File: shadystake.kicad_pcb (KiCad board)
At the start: 2 copper layers, 127 x 76.2 mm, 7 parts, among them J1 6P6C, J2 6P6C, J3 6P6C, J4 6P6C, J5 6P6C, J6 6P6C, J7 8P8C

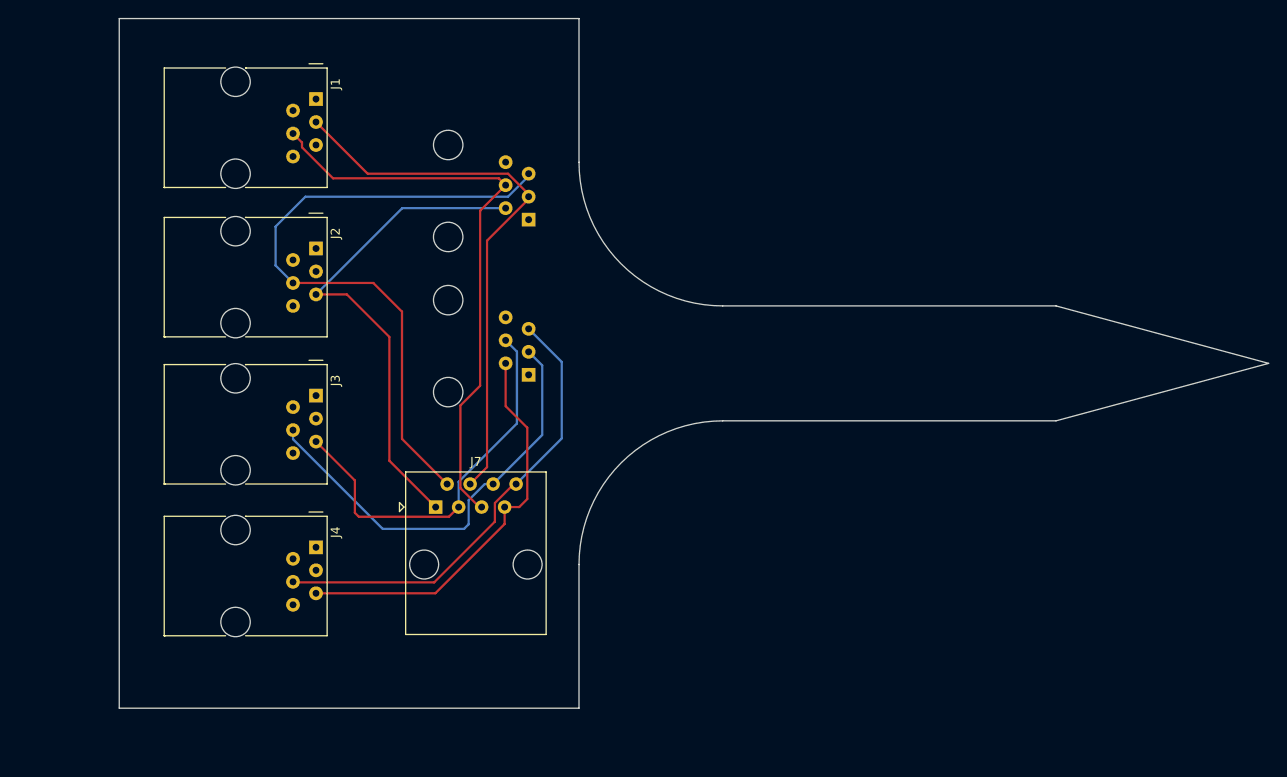
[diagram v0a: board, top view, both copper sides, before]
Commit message: shadystake: make it roughly the proportions of the Shadytel logo
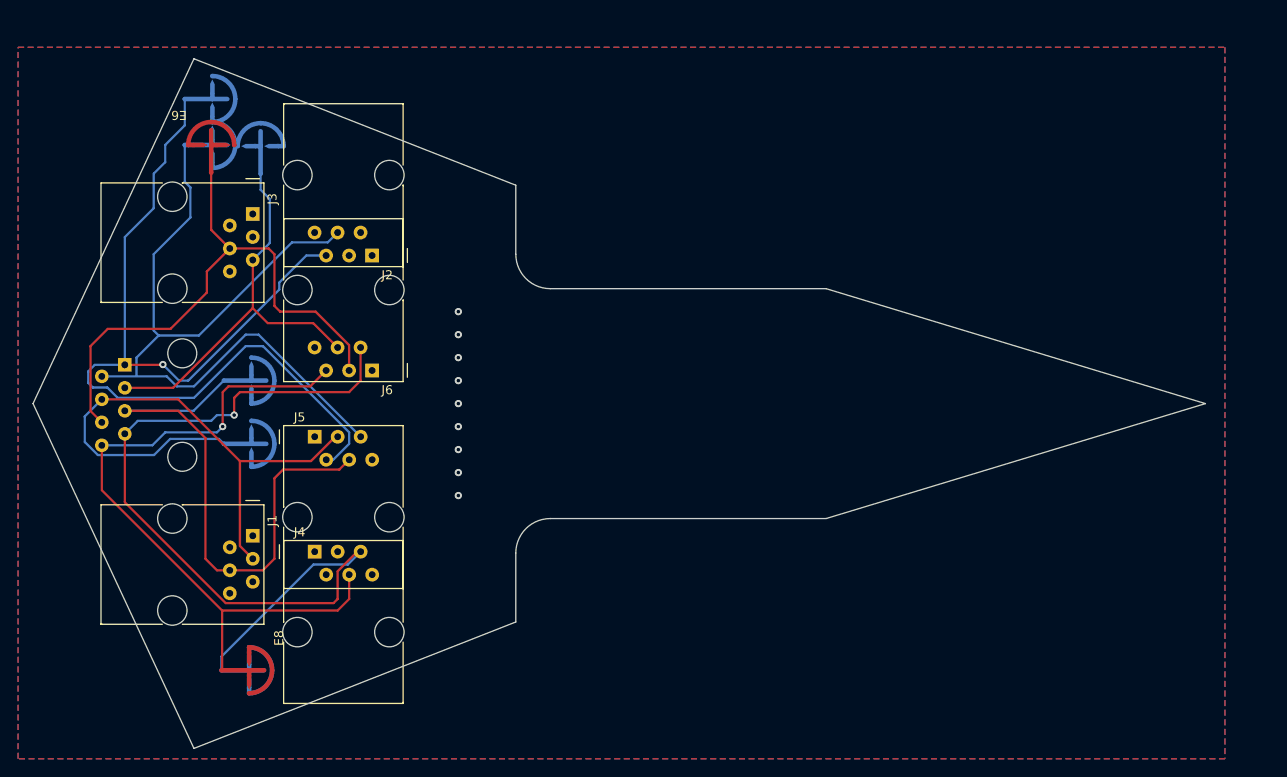
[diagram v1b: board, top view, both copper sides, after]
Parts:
- added E1: SPARK_GAP, Shadystake:Sparkgap_JLC, B.Cu at (72.4, 111.8)
- added E2: SPARK_GAP, Shadystake:Sparkgap_JLC, B.Cu at (72.4, 118.7)
- added E3: SPARK_GAP, Shadystake:Sparkgap_JLC, B.Cu at (68.1, 80.6)
- added E4: SPARK_GAP, Shadystake:Sparkgap_JLC, B.Cu at (68.1, 85.7)
- added E5: SPARK_GAP, Shadystake:Sparkgap_JLC, B.Cu at (73.4, 85.9)
- added E6: SPARK_GAP, Shadystake:Sparkgap_JLC, F.Cu at (67.9, 85.7)
- added E7: SPARK_GAP, Shadystake:Sparkgap_JLC, B.Cu at (72.1, 143.8)
- added E8: SPARK_GAP, Shadystake:Sparkgap_JLC, F.Cu at (72.1, 143.8)
- J5, J6: moved to F.Cu
- J7: moved to B.Cu
- moved J1 48.8 mm to (72.5, 128.9)
- moved J7 37.8 mm to (58.4, 110.0), turned to -90 degrees
- moved J5 33.7 mm to (79.4, 118.0), turned to 0 degrees
- moved J3 21.2 mm to (72.5, 93.3)
- moved J6 17.3 mm to (85.7, 110.6), turned to 180 degrees
- moved J2 6.24 mm to (85.7, 97.9), turned to 180 degrees
- moved J4 0.50 mm to (79.4, 130.7), turned to 0 degrees
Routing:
- net /TIP4: track 44.7 -> 97.0 mm, vias 0 -> 1
- net /TIP2: track 55.9 -> 107.3 mm, vias 0 -> 1
- net /RING4: track 50.8 -> 78.1 mm, vias 0 -> 1
- net /RING2: track 72.0 -> 89.2 mm
- net /RING3: track 48.3 -> 63.2 mm
- net /RING1: track 61.0 -> 63.5 mm
- net /TIP1: track 64.7 -> 62.5 mm
- net /TIP3: track 43.3 -> 45.0 mm
- net GND: vias 0 -> 9
- added copper zone on B.Cu, net GND
- added copper zone on F.Cu, net GND
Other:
- board size 127 x 76.2 mm -> 129.5 x 76.2 mm

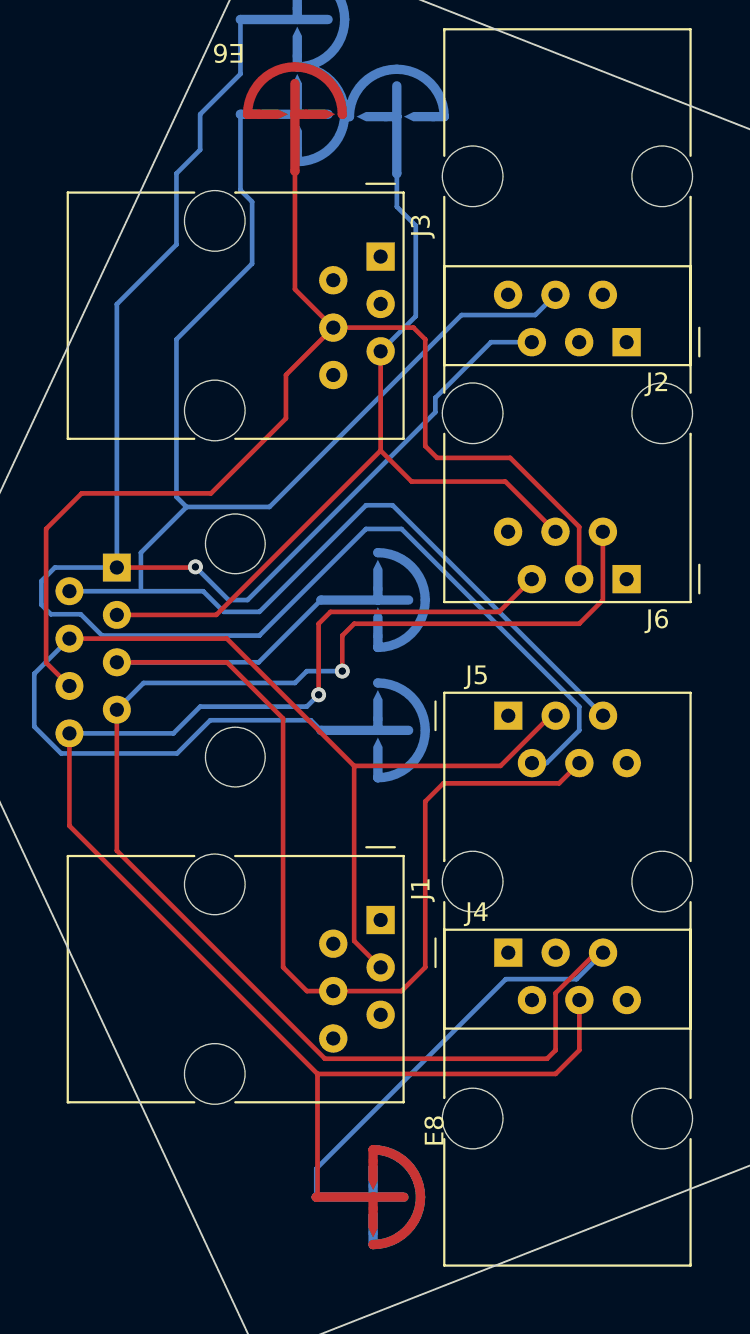
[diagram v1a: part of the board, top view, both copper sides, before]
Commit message: pcb: add copper labels on the "wrong" side of the board
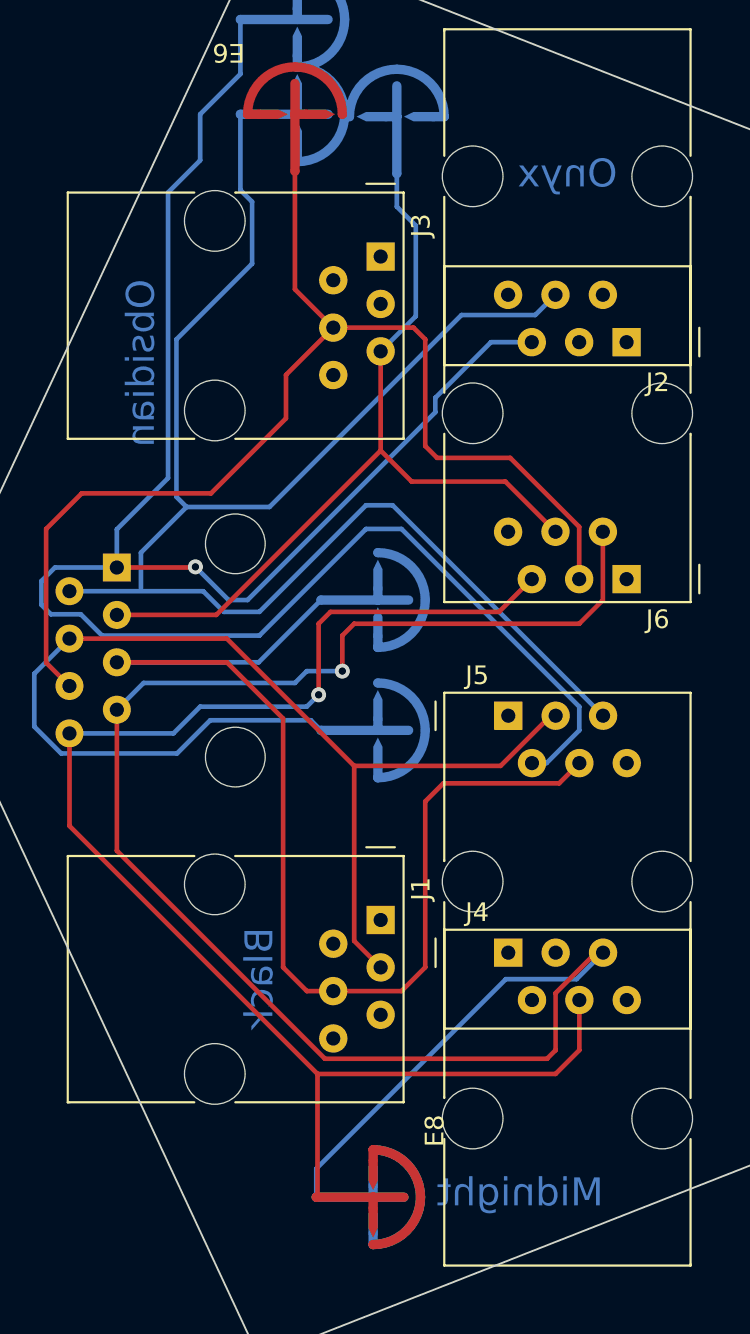
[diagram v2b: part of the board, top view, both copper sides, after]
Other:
- board text added: "Black"
- board text added: "Midnight"
- board text added: "Obsidian"
- board text added: "Onyx"
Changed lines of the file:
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@@
   (gr_arc (start 105.41 101.6) (mid 102.715923 100.484077) (end 101.6 97.79) (layer "Edge.Cuts") (width 0.1))
   (gr_line (start 101.6 130.81) (end 101.6 138.43) (layer "Edge.Cuts") (width 0.1))
+  (gr_text "Obsidian" (at 59.69 99.06 90) (layer "B.Cu")
+    (effects (font (size 1.5 1.5) (thickness 0.3)) (justify mirror))
+  )
+  (gr_text "Black" (at 66.04 132.08 90) (layer "B.Cu")
+    (effects (font (size 1.5 1.5) (thickness 0.3)) (justify mirror))
+  )
+  (gr_text "Midnight" (at 80.01 143.51) (layer "B.Cu")
+    (effects (font (size 1.5 1.5) (thickness 0.3)) (justify mirror))
+  )
+  (gr_text "Onyx" (at 82.55 88.9) (layer "B.Cu")
+    (effects (font (size 1.5 1.5) (thickness 0.3)) (justify mirror))
+  )
   (segment (start 78.966269 120.65) (end 71.12 120.65) (width 0.25) (layer "F.Cu") (net 3))
   (segment (start 81.656269 117.96) (end 78.966269 120.65) (width 0.25) (layer "F.Cu") (net 3))
@@
   (segment (start 62.611 109.982) (end 62.5755 110.0175) (width 0.25) (layer "F.Cu") (net 11))
   (via (at 62.611 109.982) (size 0.8) (drill 0.4) (layers "F.Cu" "B.Cu") (net 11))
+  (segment (start 61.14548 105.22452) (end 61.14548 89.915644) (width 0.25) (layer "B.Cu") (net 11))
   (segment (start 57.608067 113.665) (end 56.465067 112.522) (width 0.25) (layer "B.Cu") (net 11))
+  (segment (start 62.865 85.725) (end 65.024 83.566) (width 0.25) (layer "B.Cu") (net 11))
   (segment (start 78.452249 97.94) (end 75.470479 100.92177) (width 0.25) (layer "B.Cu") (net 11))
   (segment (start 64.389 111.76) (end 62.611 109.982) (width 0.25) (layer "B.Cu") (net 11))
   (segment (start 83.185 117.475) (end 73.66 107.95) (width 0.25) (layer "B.Cu") (net 11))
+  (segment (start 58.4 110.0175) (end 58.4 107.97) (width 0.25) (layer "B.Cu") (net 11))
   (segment (start 66.04 113.665) (end 57.608067 113.665) (width 0.25) (layer "B.Cu") (net 11))
-  (segment (start 62.865 87.63) (end 62.865 85.725) (width 0.25) (layer "B.Cu") (net 11))
+  (segment (start 58.4 107.97) (end 61.14548 105.22452) (width 0.25) (layer "B.Cu") (net 11))
   (segment (start 71.755 107.95) (end 66.04 113.665) (width 0.25) (layer "B.Cu") (net 11))
-  (segment (start 61.595 92.71) (end 61.595 88.9) (width 0.25) (layer "B.Cu") (net 11))
   (segment (start 56.465067 112.522) (end 54.864 112.522) (width 0.25) (layer "B.Cu") (net 11))
+  (segment (start 65.024 83.566) (end 65.024 80.645) (width 0.25) (layer "B.Cu") (net 11))
   (segment (start 75.470479 100.92177) (end 75.470479 101.694521) (width 0.25) (layer "B.Cu") (net 11))
-  (segment (start 58.4 110.0175) (end 58.4 95.905) (width 0.25) (layer "B.Cu") (net 11))
   (segment (start 54.864 112.522) (end 54.356 112.014) (width 0.25) (layer "B.Cu") (net 11))
-  (segment (start 61.595 88.9) (end 62.865 87.63) (width 0.25) (layer "B.Cu") (net 11))
   (segment (start 54.356 112.014) (end 54.356 110.744) (width 0.25) (layer "B.Cu") (net 11))
   (segment (start 81.43 120.5) (end 83.185 118.745) (width 0.25) (layer "B.Cu") (net 11))
@@
   (segment (start 80.65 120.5) (end 81.43 120.5) (width 0.25) (layer "B.Cu") (net 11))
   (segment (start 80.64 97.94) (end 78.452249 97.94) (width 0.25) (layer "B.Cu") (net 11))
-  (segment (start 58.4 95.905) (end 61.595 92.71) (width 0.25) (layer "B.Cu") (net 11))
-  (segment (start 65.024 83.566) (end 65.024 80.645) (width 0.25) (layer "B.Cu") (net 11))
-  (segment (start 62.865 85.725) (end 65.024 83.566) (width 0.25) (layer "B.Cu") (net 11))
   (segment (start 75.470479 101.694521) (end 65.405 111.76) (width 0.25) (layer "B.Cu") (net 11))
+  (segment (start 62.865 88.196124) (end 62.865 85.725) (width 0.25) (layer "B.Cu") (net 11))
   (segment (start 83.185 118.745) (end 83.185 117.475) (width 0.25) (layer "B.Cu") (net 11))
   (segment (start 65.405 111.76) (end 64.389 111.76) (width 0.25) (layer "B.Cu") (net 11))
   (segment (start 54.356 110.744) (end 55.0825 110.0175) (width 0.25) (layer "B.Cu") (net 11))
   (segment (start 73.66 107.95) (end 71.755 107.95) (width 0.25) (layer "B.Cu") (net 11))
+  (segment (start 61.14548 89.915644) (end 62.865 88.196124) (width 0.25) (layer "B.Cu") (net 11))
   (segment (start 83.18 107.836269) (end 83.18 110.64) (width 0.25) (layer "F.Cu") (net 16))
   (segment (start 75.565 104.14) (end 79.483731 104.14) (width 0.25) (layer "F.Cu") (net 16))

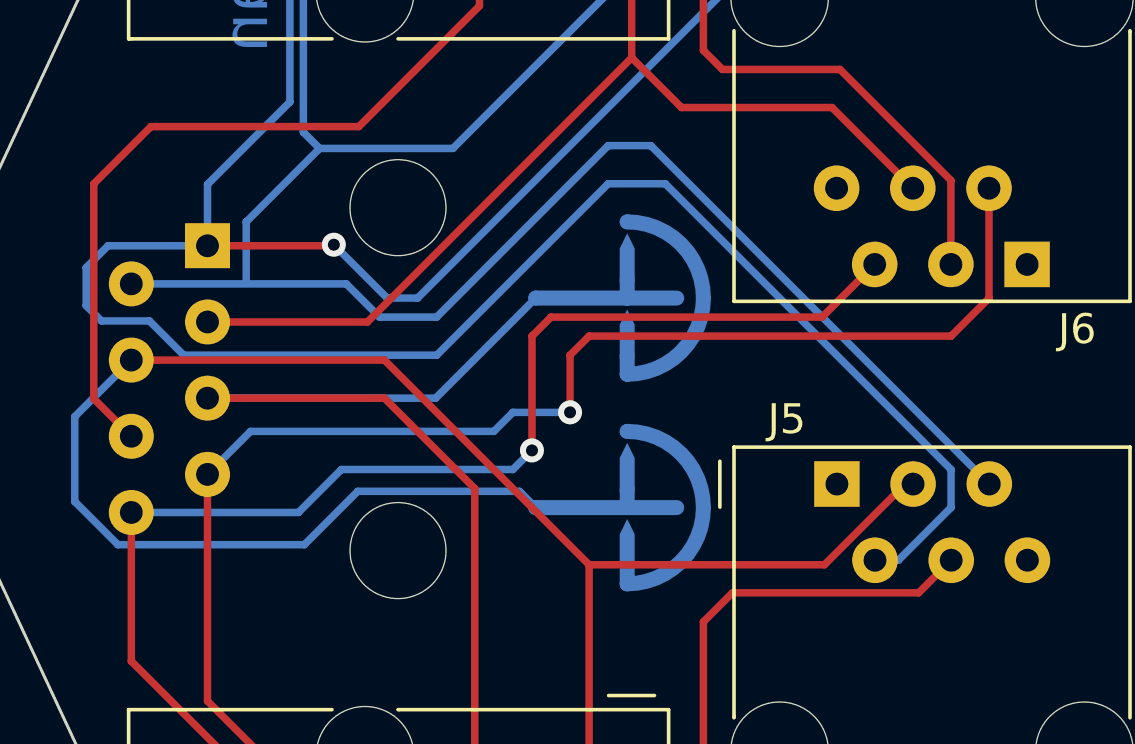
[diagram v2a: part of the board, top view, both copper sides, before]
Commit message: Gerber export settings and one minor reroute.
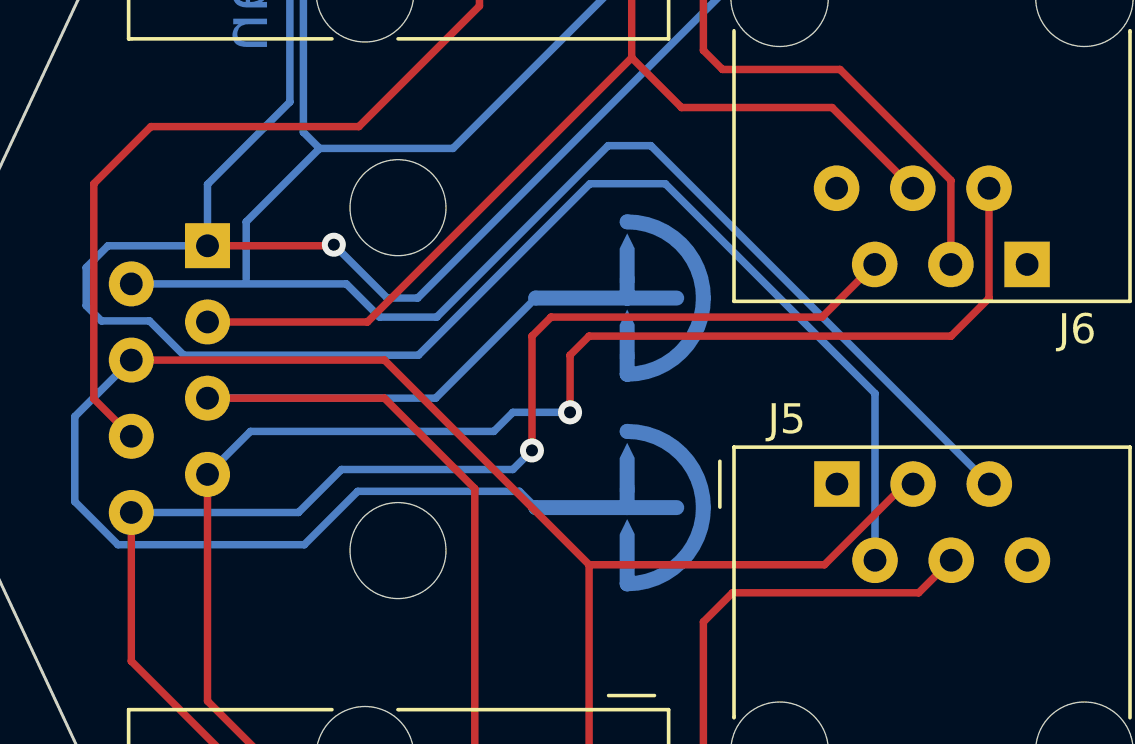
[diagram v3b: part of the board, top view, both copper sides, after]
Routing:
- net /TIP2: track 107.3 -> 104.7 mm
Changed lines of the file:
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@@
       (layerselection 0x00010fc_ffffffff)
       (disableapertmacros false)
-      (usegerberextensions false)
+      (usegerberextensions true)
       (usegerberattributes true)
-      (usegerberadvancedattributes true)
-      (creategerberjobfile true)
+      (usegerberadvancedattributes false)
+      (creategerberjobfile false)
       (svguseinch false)
       (svgprecision 6)
@@
       (psnegative false)
       (psa4output false)
-      (plotreference true)
-      (plotvalue true)
+      (plotreference false)
+      (plotvalue false)
       (plotinvisibletext false)
       (sketchpadsonfab false)
-      (subtractmaskfromsilk false)
+      (subtractmaskfromsilk true)
       (outputformat 1)
       (mirror false)
-      (drillshape 1)
+      (drillshape 0)
       (scaleselection 1)
-      (outputdirectory "")
+      (outputdirectory "shadystakev01")
     )
   )
@@
   (via (at 62.611 109.982) (size 0.8) (drill 0.4) (layers "F.Cu" "B.Cu") (net 11))
   (segment (start 61.14548 105.22452) (end 61.14548 89.915644) (width 0.25) (layer "B.Cu") (net 11))
-  (segment (start 57.608067 113.665) (end 56.465067 112.522) (width 0.25) (layer "B.Cu") (net 11))
+  (segment (start 80.65 120.5) (end 80.65 114.94) (width 0.25) (layer "B.Cu") (net 11))
   (segment (start 62.865 85.725) (end 65.024 83.566) (width 0.25) (layer "B.Cu") (net 11))
   (segment (start 78.452249 97.94) (end 75.470479 100.92177) (width 0.25) (layer "B.Cu") (net 11))
+  (segment (start 57.608067 113.665) (end 56.465067 112.522) (width 0.25) (layer "B.Cu") (net 11))
+  (segment (start 73.66 107.95) (end 71.146372 107.95) (width 0.25) (layer "B.Cu") (net 11))
   (segment (start 64.389 111.76) (end 62.611 109.982) (width 0.25) (layer "B.Cu") (net 11))
-  (segment (start 83.185 117.475) (end 73.66 107.95) (width 0.25) (layer "B.Cu") (net 11))
   (segment (start 58.4 110.0175) (end 58.4 107.97) (width 0.25) (layer "B.Cu") (net 11))
-  (segment (start 66.04 113.665) (end 57.608067 113.665) (width 0.25) (layer "B.Cu") (net 11))
   (segment (start 58.4 107.97) (end 61.14548 105.22452) (width 0.25) (layer "B.Cu") (net 11))
-  (segment (start 71.755 107.95) (end 66.04 113.665) (width 0.25) (layer "B.Cu") (net 11))
-  (segment (start 56.465067 112.522) (end 54.864 112.522) (width 0.25) (layer "B.Cu") (net 11))
+  (segment (start 65.431372 113.665) (end 57.608067 113.665) (width 0.25) (layer "B.Cu") (net 11))
+  (segment (start 55.0825 110.0175) (end 58.4 110.0175) (width 0.25) (layer "B.Cu") (net 11))
+  (segment (start 71.146372 107.95) (end 65.431372 113.665) (width 0.25) (layer "B.Cu") (net 11))
   (segment (start 65.024 83.566) (end 65.024 80.645) (width 0.25) (layer "B.Cu") (net 11))
   (segment (start 75.470479 100.92177) (end 75.470479 101.694521) (width 0.25) (layer "B.Cu") (net 11))
+  (segment (start 54.356 112.014) (end 54.356 110.744) (width 0.25) (layer "B.Cu") (net 11))
+  (segment (start 80.64 97.94) (end 78.452249 97.94) (width 0.25) (layer "B.Cu") (net 11))
+  (segment (start 54.356 110.744) (end 55.0825 110.0175) (width 0.25) (layer "B.Cu") (net 11))
+  (segment (start 75.470479 101.694521) (end 65.405 111.76) (width 0.25) (layer "B.Cu") (net 11))
   (segment (start 54.864 112.522) (end 54.356 112.014) (width 0.25) (layer "B.Cu") (net 11))
-  (segment (start 54.356 112.014) (end 54.356 110.744) (width 0.25) (layer "B.Cu") (net 11))
-  (segment (start 81.43 120.5) (end 83.185 118.745) (width 0.25) (layer "B.Cu") (net 11))
-  (segment (start 55.0825 110.0175) (end 58.4 110.0175) (width 0.25) (layer "B.Cu") (net 11))
-  (segment (start 80.65 120.5) (end 81.43 120.5) (width 0.25) (layer "B.Cu") (net 11))
-  (segment (start 80.64 97.94) (end 78.452249 97.94) (width 0.25) (layer "B.Cu") (net 11))
-  (segment (start 75.470479 101.694521) (end 65.405 111.76) (width 0.25) (layer "B.Cu") (net 11))
   (segment (start 62.865 88.196124) (end 62.865 85.725) (width 0.25) (layer "B.Cu") (net 11))
-  (segment (start 83.185 118.745) (end 83.185 117.475) (width 0.25) (layer "B.Cu") (net 11))
+  (segment (start 80.65 114.94) (end 73.66 107.95) (width 0.25) (layer "B.Cu") (net 11))
   (segment (start 65.405 111.76) (end 64.389 111.76) (width 0.25) (layer "B.Cu") (net 11))
-  (segment (start 54.356 110.744) (end 55.0825 110.0175) (width 0.25) (layer "B.Cu") (net 11))
-  (segment (start 73.66 107.95) (end 71.755 107.95) (width 0.25) (layer "B.Cu") (net 11))
   (segment (start 61.14548 89.915644) (end 62.865 88.196124) (width 0.25) (layer "B.Cu") (net 11))
+  (segment (start 56.465067 112.522) (end 54.864 112.522) (width 0.25) (layer "B.Cu") (net 11))
   (segment (start 83.18 107.836269) (end 83.18 110.64) (width 0.25) (layer "F.Cu") (net 16))
   (segment (start 75.565 104.14) (end 79.483731 104.14) (width 0.25) (layer "F.Cu") (net 16))
